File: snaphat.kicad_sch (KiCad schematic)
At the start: 94 parts, among them J1 Conn_01x08_S8B-PH-K-S(LF)(SN), J10 P70-6000045R, J11 P70-6000045R, J12 P70-6000045R, J2 Conn_02x20_2214SM-40G-75-PCR, J3 Conn_01x02_B2B-PH-K-S(LF)(SN), J4 USB_C_USB4930-00-A, J5 Conn_01x03_MC34747, J6 Conn_01x04_SFV4R-3STBE1HLF/C, J7 Conn_01x04_SFV4R-3STBE1HLF/C, J8 P70-6000045R, J9 P70-6000045R, Q1 Q_BC817-25, SW1 SW_B3FS-1050, SW2 SW_B3FS-1050, SW3 SW_B3FS-1050, SW4 SW_B3FS-1050, SW5 SW_B3FS-1050, SW6 SW_B3FS-1050, SW7 SW_B3FS-1050, SW8 SW_B3F-3150, U4 TPD2EUSB30DRTR, U6 LIS2DW12TR

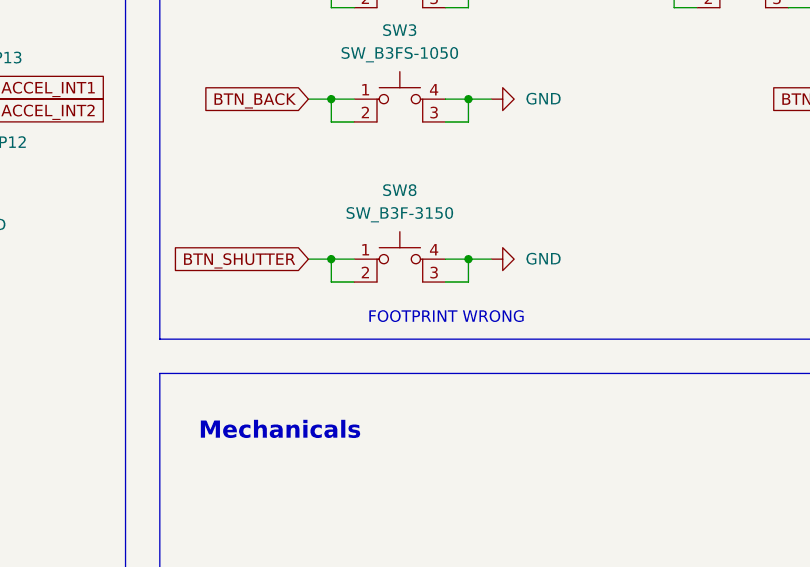
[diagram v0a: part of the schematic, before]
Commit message: Fix B3F-3150 symbol
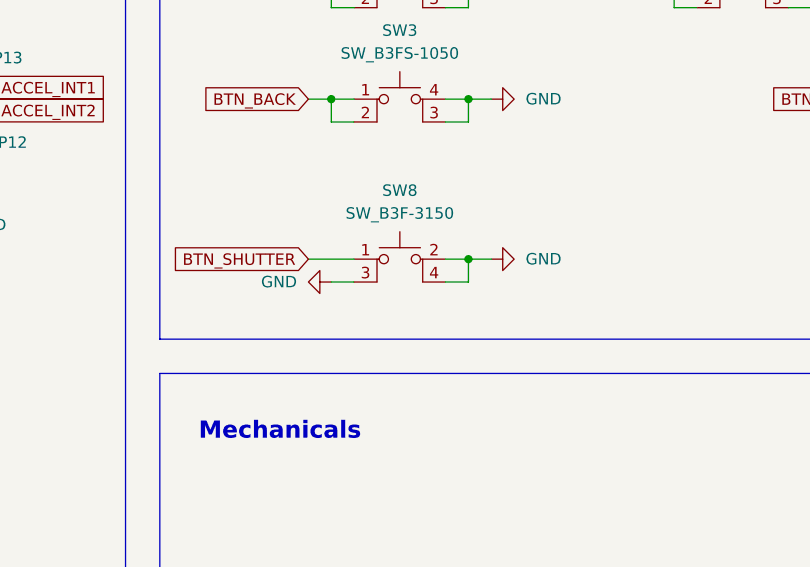
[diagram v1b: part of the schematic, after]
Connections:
- net BTN_SHUTTER: no longer SW8.2
- net GND: now also SW8.2
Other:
- note removed: "FOOTPRINT WRONG"
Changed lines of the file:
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@@
 		)
 	)
-	(text "FOOTPRINT WRONG"
-		(exclude_from_sim no)
-		(at 112.014 247.396 0)
-		(effects
-			(font
-				(face "Quicksand")
-				(size 1.27 1.27)
-				(thickness 0.1588)
-				(color 42 101 127 1)
-			)
-			(justify left bottom)
-		)
-	)
 	(text "GPIO9(MISO)\n"
 		(exclude_from_sim no)
@@
 	)
 	(junction
-		(at 107.95 240.03)
-		(diameter 0)
-		(color 38 87 104 1)
-	)
-	(junction
 		(at 69.85 213.36)
 		(diameter 0)
@@
 	(wire
 		(pts
-			(xy 105.41 240.03) (xy 107.95 240.03)
-		)
-		(stroke
-			(width 0)
-			(type solid)
-			(color 132 0 0 1)
-		)
-	)
-	(wire
-		(pts
 			(xy 284.48 67.31) (xy 287.02 67.31)
 		)
@@
 	(wire
 		(pts
-			(xy 107.95 240.03) (xy 110.49 240.03)
+			(xy 105.41 240.03) (xy 110.49 240.03)
 		)
 		(stroke
@@
 	(wire
 		(pts
-			(xy 107.95 242.57) (xy 107.95 240.03)
-		)
-		(stroke
-			(width 0)
-			(type solid)
-			(color 132 0 0 1)
-		)
-	)
-	(wire
-		(pts
 			(xy 93.98 86.36) (xy 111.76 86.36)
 		)
@@
 	)
 	(symbol
+		(lib_id "power:GND")
+		(at 107.95 242.57 270)
+		(unit 1)
+		(exclude_from_sim no)
+		(in_bom yes)
+		(on_board yes)
+		(dnp no)
+		(fields_autoplaced yes)
+		(property "Reference" "#PWR037"
+			(at 101.6 242.57 0)
+			(effects
+				(font
+					(face "Quicksand")
+					(size 1.27 1.27)
+					(color 42 101 127 1)
+				)
+				(hide yes)
+			)
+		)
+		(property "Value" "GND"
+			(at 104.14 242.5699 90)
+			(effects
+				(font
+					(face "Quicksand")
+					(size 1.27 1.27)
+					(color 42 101 127 1)
+				)
+				(justify right)
+			)
+		)
+		(property "Footprint" ""
+			(at 107.95 242.57 0)
+			(effects
+				(font
+					(face "Quicksand")
+					(size 1.27 1.27)
+					(color 42 101 127 1)
+				)
+				(hide yes)
+			)
+		)
+		(property "Datasheet" ""
+			(at 107.95 242.57 0)
+			(effects
+				(font
+					(face "Quicksand")
+					(size 1.27 1.27)
+					(color 42 101 127 1)
+				)
+				(hide yes)
+			)
+		)
+		(property "Description" "Power symbol creates a global label with name \"GND\" , ground"
+			(at 107.95 242.57 0)
+			(effects
+				(font
+					(face "Quicksand")
+					(size 1.27 1.27)
+					(color 42 101 127 1)
+				)
+				(hide yes)
+			)
+		)
+		(pin "1"
+		)
+		(instances
+			(project "snaphat"
+				(path "/1b9269fa-3ac8-429a-ab83-4cc9a4203d51"
+					(reference "#PWR037")
+					(unit 1)
+				)
+			)
+		)
+	)
+	(symbol
 		(lib_id "library:B32-2010")
 		(at 200.66 240.03 0)
@@
 	)
 	(symbol
+		(lib_id "library:SW_B3F-3150")
+		(at 115.57 240.03 0)
+		(unit 1)
+		(exclude_from_sim no)
+		(in_bom yes)
+		(on_board yes)
+		(dnp no)
+		(fields_autoplaced yes)
+		(property "Reference" "SW8"
+			(at 115.57 232.41 0)
+			(effects
+				(font
+					(size 1.27 1.27)
+				)
+			)
+		)
+		(property "Value" "SW_B3F-3150"
+			(at 115.57 234.95 0)
+			(effects
+				(font
+					(size 1.27 1.27)
+				)
+			)
+		)
+		(property "Footprint" "library:SW_B3F-3150"
+			(at 115.57 240.03 0)
+			(effects
+				(font
+					(size 1.27 1.27)
+				)
+				(hide yes)
+			)
+		)
+		(property "Datasheet" ""
+			(at 115.57 240.03 0)
+			(effects
+				(font
+					(size 1.27 1.27)
+				)
+				(hide yes)
+			)
+		)
+		(property "Description" "Tactile Switch, B3D Series, Side Actuated, Through Hole, Plunger for Cap, 100 gf, 50mA at 24VDC"
+			(at 115.57 240.03 0)
+			(effects
+				(font
+					(size 1.27 1.27)
+				)
+				(hide yes)
+			)
+		)
+		(property "Part number" "B3F-3150"
+			(at 115.57 240.03 0)
+			(effects
+				(font
+					(size 1.27 1.27)
+				)
+				(hide yes)
+			)
+		)
+		(property "Manufacturer" "OMRON"
+			(at 115.57 240.03 0)
+			(effects
+				(font
+					(size 1.27 1.27)
+				)
+				(hide yes)
+			)
+		)
+		(pin "3"
+		)
+		(pin "1"
+		)
+		(pin "2"
+		)
+		(pin "4"
+		)
+		(instances
+			(project ""
+				(path "/1b9269fa-3ac8-429a-ab83-4cc9a4203d51"
+					(reference "SW8")
+					(unit 1)
+				)
+			)
+		)
+	)
+	(symbol
 		(lib_id "library:1386735")
 		(at 186.69 267.97 0)
@@
 					(unit 1)
 				)
-			)
-		)
-	)
-	(symbol
-		(lib_id "library:SW_B3F-3150")
-		(at 115.57 242.57 0)
-		(unit 1)
-		(exclude_from_sim no)
-		(in_bom yes)
-		(on_board yes)
-		(dnp no)
-		(fields_autoplaced yes)
-		(property "Reference" "SW8"
-			(at 115.57 232.41 0)
-			(effects
-				(font
-					(face "Quicksand")
-					(size 1.27 1.27)
-					(color 42 101 127 1)
-				)
-			)
-		)
-		(property "Value" "SW_B3F-3150"
-			(at 115.57 234.95 0)
-			(effects
-				(font
-					(face "Quicksand")
-					(size 1.27 1.27)
-					(color 42 101 127 1)
-				)
-			)
-		)
-		(property "Footprint" "library:SW_B3F-3150"
-			(at 115.57 234.95 0)
-			(effects
-				(font
-					(face "Quicksand")
-					(size 1.27 1.27)
-					(color 42 101 127 1)
-				)
-				(hide yes)
-			)
-		)
-		(property "Datasheet" "http://www.apem.com/int/index.php?controller=attachment&id_attachment=1371"
-			(at 115.57 234.95 0)
-			(effects
-				(font
-					(face "Quicksand")
-					(size 1.27 1.27)
-					(color 42 101 127 1)
-				)
-				(hide yes)
-			)
-		)
-		(property "Description" "Tactile Switch, B3D Series, Side Actuated, Through Hole, Plunger for Cap, 100 gf, 50mA at 24VDC"
-			(at 115.57 242.57 0)
-			(effects
-				(font
-					(face "Quicksand")
-					(size 1.27 1.27)
-					(color 42 101 127 1)
-				)
-				(hide yes)
-			)
-		)
-		(property "Part number" "B3F-3150"
-			(at 115.57 242.57 0)
-			(effects
-				(font
-					(face "Quicksand")
-					(size 1.27 1.27)
-					(color 42 101 127 1)
-				)
-				(hide yes)
-			)
-		)
-		(property "Manufacturer" "OMRON"
-			(at 115.57 242.57 0)
-			(effects
-				(font
-					(face "Quicksand")
-					(size 1.27 1.27)
-					(color 42 101 127 1)
-				)
-				(hide yes)
-			)
-		)
-		(property "Part name" ""
-			(at 115.57 242.57 0)
-			(effects
-				(font
-					(size 1.27 1.27)
-				)
-			)
-		)
-		(pin "2"
-		)
-		(pin "3"
-		)
-		(pin "1"
-		)
-		(pin "4"
-		)
-		(instances
-			(project ""
-				(path "/1b9269fa-3ac8-429a-ab83-4cc9a4203d51"
-					(reference "SW8")
-					(unit 1)
-				)

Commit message: Fixes to power charger, cleanup schematic
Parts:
- added H15: 10304, library:Li-Pol_battery_8x30x40mm, symbol library:10304
- added H48, H49: SPH-002T-P0.5S, symbol library:SPH-002T-P0.5S
- added H50: PHR-2, symbol library:PHR-2
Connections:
- net BUZZER_SIGNAL is gone; now on net GND: J2.12 (Pin_12), R1.1
- net DISPLAY_BL is gone; now on net GND: J1.8 (Pin_8), J2.32 (Pin_32), R28.1
- net DISPLAY_DC is gone; now on net GND: J1.6 (Pin_6), J2.22 (Pin_22)
- net DISPLAY_RST is gone; now on net GND: J1.7 (Pin_7), J2.18 (Pin_18)
- net DISPLAY_SPI_CS is gone; now on net GND: J1.5 (Pin_5), J2.24 (Pin_24)
- net RPI_UART_RX is gone; now on net GND: J2.10 (Pin_10), J5.1 (Pin_1)
- net RPI_UART_TX is gone; now on net GND: J2.8 (Pin_8), J5.2 (Pin_2)
- net BTN_D: now also J2.27 (Pin_27); no longer J2.29 (Pin_29)
- net BTN_L: now also J2.29 (Pin_29); no longer J2.31 (Pin_31)
- net BTN_R: now also J2.31 (Pin_31); no longer J2.33 (Pin_33)
- net BTN_U: now also J2.33 (Pin_33); no longer J2.35 (Pin_35)
- net BTN_BACK renamed BTN_B
- net BTN_OK renamed BTN_A
- net DISPLAY_SPI_MOSI renamed DISPLAY_MOSI
- new net LOW_BATTERY: J2.35 (Pin_35)
- no-connect marks 10 -> 8
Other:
- note added: "Camera module:"
- note added: "Li-Po battery:"
- note added: "Raspberry Pi header"
- note added: "RaspberryPi spacers:"
- note added: "RaspberryPi:"
- note added: "USB-C and battery connector"
- note removed: "Raspberry Pi header and USB OTG"
- moved on the sheet: BZ1, C15, C19, C2, C20, C9, D1, D7, D8, H1, H10, H11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

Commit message: Start updating PCB, library fixes
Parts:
- removed H33: 9774100151R, library:Mounting_Wuerth_WA-SMSI-M2.5_H10mm_9774100151R, symbol library:9774100151R
- J4: footprint (none) -> library:USB_C_Receptacle_GCT_USB4105-xx-A_16P_TopMnt_Horizontal
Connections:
- net GND: now also J6.1 (Pin_1); no longer J6.4 (Pin_4)
- net GND_EXT: now also J7.1 (Pin_1); no longer J7.4 (Pin_4)
- net USBC_DATA_N: now also J6.3 (Pin_3); no longer J6.2 (Pin_2)
- net USBC_DATA_P: now also J6.2 (Pin_2); no longer J6.3 (Pin_3)
- net USBC_EXT_DATA_N: now also J7.3 (Pin_3); no longer J7.2 (Pin_2)
- net USBC_EXT_DATA_P: now also J7.2 (Pin_2); no longer J7.3 (Pin_3)
- net VBUS_EXT: now also J7.4 (Pin_4); no longer J7.1 (Pin_1)
- net BATTERY_N renamed Power supply/BATTERY_N
- net BATTERY_P renamed Power supply/BATTERY_P
- net PM_SCL renamed I2C_SCL
- net PM_SDA renamed I2C_SDA
- net VBUS renamed Power supply/VBUS
- net Power supply/VBUS: now also J6.4 (Pin_4); no longer J6.1 (Pin_1)
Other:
- sheet Power supply ports: added 3V3, 5V0, BATTERY_N, BATTERY_P, LOW_BATTERY, PM_SCL, PM_SDA, VBUS; removed none
- moved on the sheet: J7, SW1, SW2, SW3, SW4, SW5, SW6, SW7, SW8

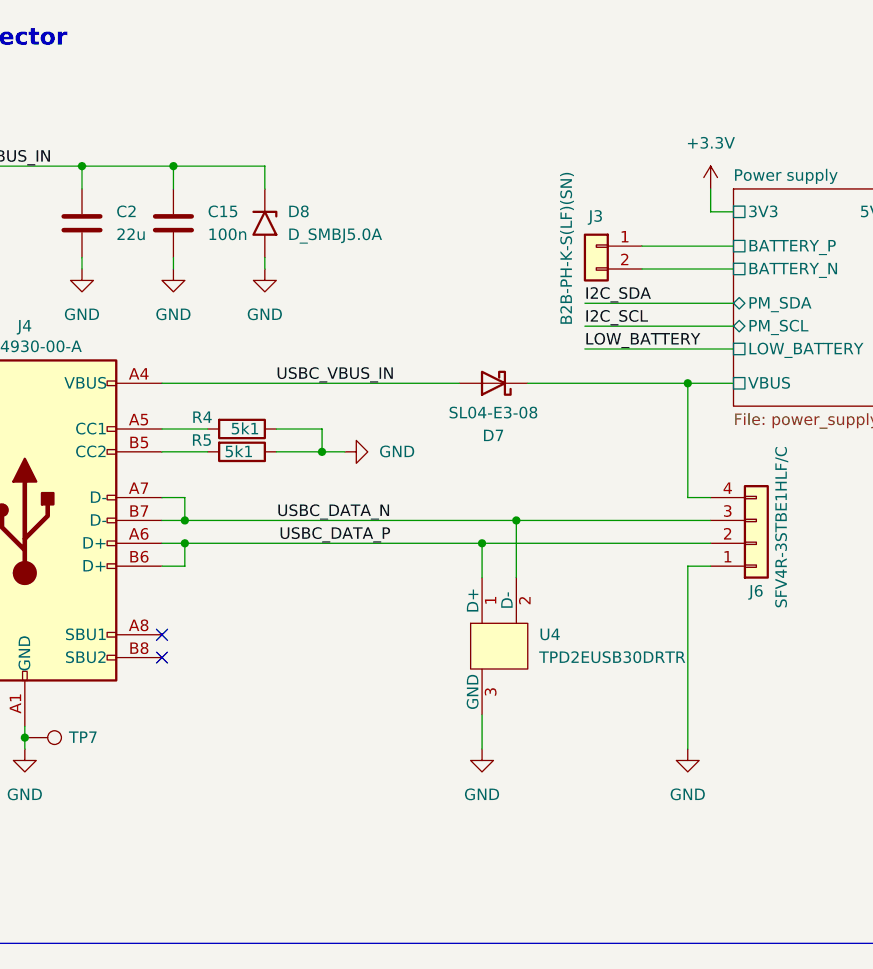
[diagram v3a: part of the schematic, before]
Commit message: Rerouted power and USB
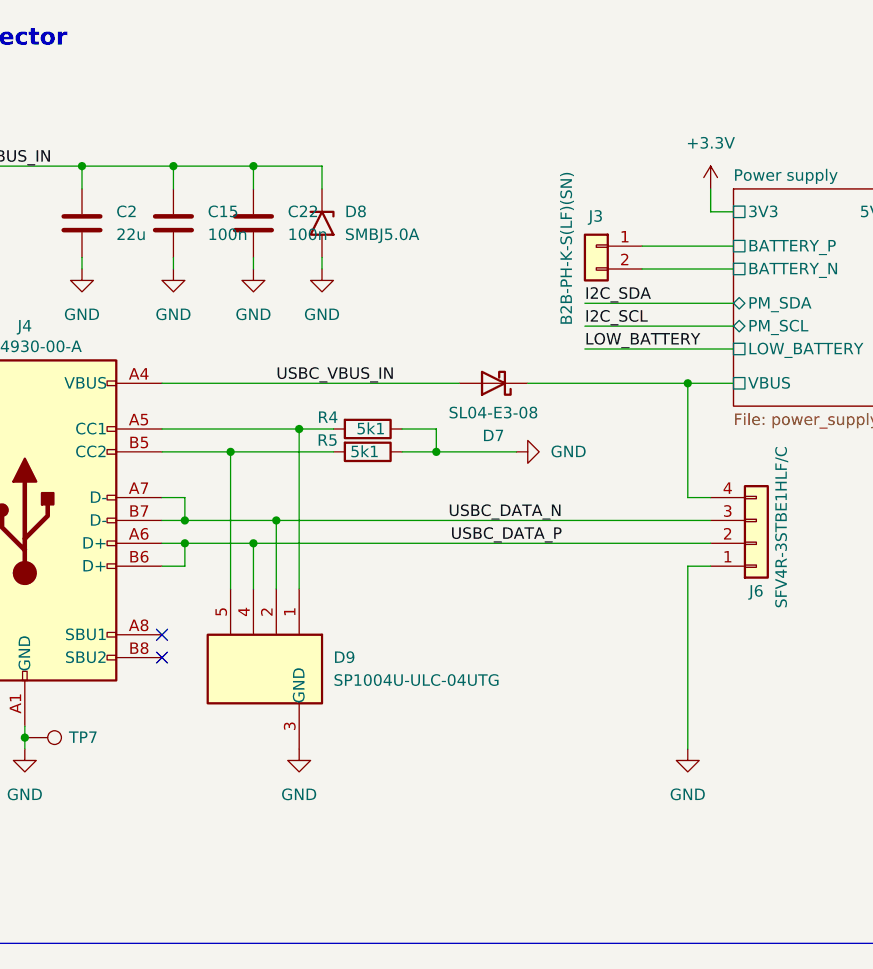
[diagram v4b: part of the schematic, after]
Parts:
- removed U4: TPD2EUSB30DRTR, library:Texas_DRT-3, symbol library:TPD2EUSB30DRTR
- added C22: 100n, library:C_0402_1005Metric, symbol library:C_100n_0402
- added D9: SP1004U-ULC-04UTG, library:SP1004UULC04UTG, symbol library:SP1004U-ULC-04UTG
- D8: footprint library:D_SMB -> library:SOD-123FL; symbol library:SMBJ5.0A -> library:D_SMF5.0A
- J1: footprint library:DW08R -> library:JST_S8B-PH-K-S_LF__SN_
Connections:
- net GND: now also C22.1, D9.3 (GND), D9.8 (GND_2)
- net USBC_DATA_N: now also D9.2, D9.9 (NC_3)
- net USBC_DATA_P: now also D9.4, D9.7 (NC_2)
- net USBC_VBUS_IN: now also C22.2
- net at J4.A5 (CC1), R4.2: now also D9.1, D9.10 (NC_4)
- net at J4.B5 (CC2), R5.2: now also D9.5, D9.6 (NC_1)
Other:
- moved on the sheet: D8, R4, R5

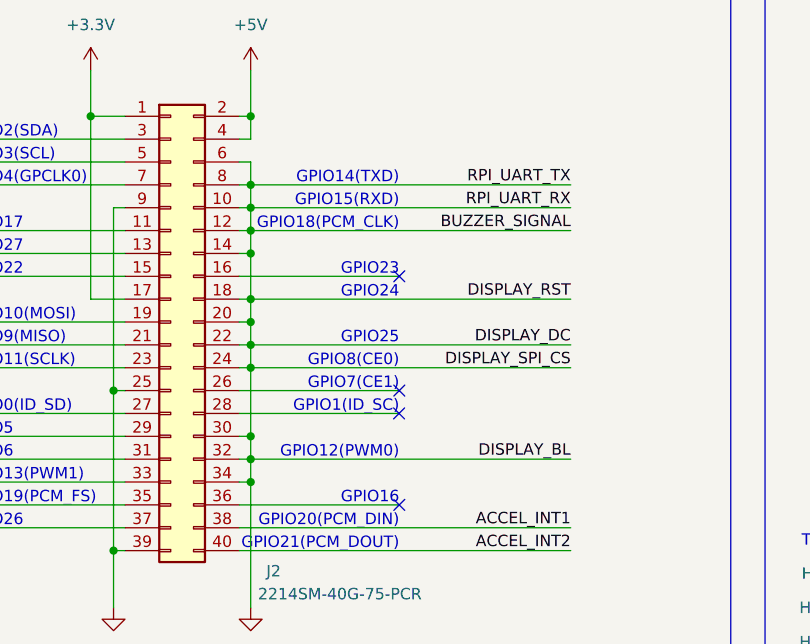
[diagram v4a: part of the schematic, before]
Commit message: Fix RPi connector on schematic, route rest of signals
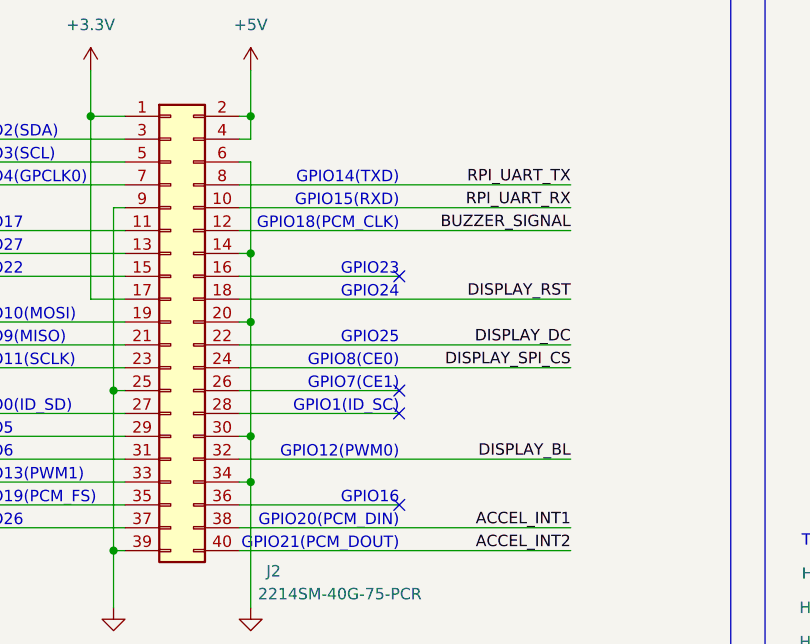
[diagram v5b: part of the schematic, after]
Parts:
- J1: footprint library:JST_S8B-PH-K-S_LF__SN_ -> library:DW08R
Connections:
- net GND: no longer J1.5 (Pin_5), J1.6 (Pin_6), J1.7 (Pin_7), J1.8 (Pin_8), J2.10 (Pin_10), J2.12 (Pin_12), J2.18 (Pin_18), J2.22 (Pin_22), J2.24 (Pin_24), J2.32 (Pin_32), J2.8 (Pin_8), J5.1 (Pin_1), J5.2 (Pin_2), R1.1, R28.1
- new net BUZZER_SIGNAL: J2.12 (Pin_12), R1.1
- new net DISPLAY_BL: J1.8 (Pin_8), J2.32 (Pin_32), R28.1
- new net DISPLAY_DC: J1.6 (Pin_6), J2.22 (Pin_22)
- new net DISPLAY_RST: J1.7 (Pin_7), J2.18 (Pin_18)
- new net DISPLAY_SPI_CS: J1.5 (Pin_5), J2.24 (Pin_24)
- new net RPI_UART_RX: J2.10 (Pin_10), J5.1 (Pin_1)
- new net RPI_UART_TX: J2.8 (Pin_8), J5.2 (Pin_2)
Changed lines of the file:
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@@
 	)
 	(junction
-		(at 161.29 173.99)
-		(diameter 0)
-		(color 0 0 0 0)
-	)
-	(junction
 		(at 143.51 166.37)
 		(diameter 0)
@@
 	)
 	(junction
-		(at 161.29 191.77)
-		(diameter 0)
-		(color 0 0 0 0)
-	)
-	(junction
 		(at 281.94 191.77)
 		(diameter 0)
@@
 	)
 	(junction
-		(at 161.29 179.07)
-		(diameter 0)
-		(color 0 0 0 0)
-	)
-	(junction
 		(at 378.46 199.39)
 		(diameter 0)
@@
 	)
 	(junction
-		(at 161.29 204.47)
-		(diameter 0)
-		(color 0 0 0 0)
-	)
-	(junction
 		(at 349.25 81.28)
 		(diameter 0)
@@
 	)
 	(junction
-		(at 161.29 194.31)
-		(diameter 0)
-		(color 0 0 0 0)
-	)
-	(junction
 		(at 68.58 175.26)
 		(diameter 0)
@@
 	)
 	(junction
-		(at 161.29 176.53)
-		(diameter 0)
-		(color 0 0 0 0)
-	)
-	(junction
 		(at 227.33 68.58)
 		(diameter 0)
@@
 	)
 	(junction
-		(at 161.29 186.69)
-		(diameter 0)
-		(color 0 0 0 0)
-	)
-	(junction
 		(at 68.58 172.72)
 		(diameter 0)
@@
 	(wire
 		(pts
-			(xy 161.29 191.77) (xy 160.02 191.77)
-		)
-		(stroke
-			(width 0)
-			(type solid)
-		)
-	)
-	(wire
-		(pts
-			(xy 161.29 179.07) (xy 161.29 181.61)
-		)
-		(stroke
-			(width 0)
-			(type solid)
-		)
-	)
-	(wire
-		(pts
 			(xy 378.46 196.85) (xy 378.46 199.39)
 		)
@@
 	(wire
 		(pts
-			(xy 161.29 173.99) (xy 160.02 173.99)
+			(xy 160.02 173.99) (xy 196.85 173.99)
 		)
 		(stroke
@@
 	(wire
 		(pts
-			(xy 161.29 181.61) (xy 161.29 186.69)
+			(xy 161.29 181.61) (xy 161.29 189.23)
 		)
 		(stroke
@@
 	(wire
 		(pts
-			(xy 161.29 176.53) (xy 160.02 176.53)
+			(xy 160.02 176.53) (xy 196.85 176.53)
 		)
 		(stroke
@@
 	(wire
 		(pts
-			(xy 161.29 189.23) (xy 161.29 191.77)
-		)
-		(stroke
-			(width 0)
-			(type solid)
-		)
-	)
-	(wire
-		(pts
 			(xy 35.56 180.34) (xy 33.02 180.34)
 		)
@@
 	(wire
 		(pts
-			(xy 161.29 194.31) (xy 160.02 194.31)
-		)
-		(stroke
-			(width 0)
-			(type solid)
-		)
-	)
-	(wire
-		(pts
 			(xy 284.48 213.36) (xy 284.48 210.82)
 		)
@@
 	(wire
 		(pts
-			(xy 161.29 173.99) (xy 196.85 173.99)
-		)
-		(stroke
-			(width 0)
-			(type solid)
-		)
-	)
-	(wire
-		(pts
 			(xy 214.63 36.83) (xy 214.63 39.37)
 		)
@@
 	(wire
 		(pts
-			(xy 161.29 176.53) (xy 161.29 179.07)
+			(xy 161.29 171.45) (xy 161.29 181.61)
 		)
 		(stroke
@@
 	(wire
 		(pts
-			(xy 161.29 186.69) (xy 160.02 186.69)
-		)
-		(stroke
-			(width 0)
-			(type solid)
-		)
-	)
-	(wire
-		(pts
 			(xy 255.27 144.78) (xy 269.24 144.78)
 		)
@@
 	(wire
 		(pts
-			(xy 161.29 173.99) (xy 161.29 176.53)
-		)
-		(stroke
-			(width 0)
-			(type solid)
-		)
-	)
-	(wire
-		(pts
 			(xy 269.24 147.32) (xy 266.7 147.32)
 		)
@@
 	(wire
 		(pts
-			(xy 161.29 186.69) (xy 196.85 186.69)
+			(xy 160.02 186.69) (xy 196.85 186.69)
 		)
 		(stroke
@@
 	(wire
 		(pts
-			(xy 161.29 204.47) (xy 160.02 204.47)
-		)
-		(stroke
-			(width 0)
-			(type solid)
-		)
-	)
-	(wire
-		(pts
 			(xy 281.94 39.37) (xy 281.94 41.91)
 		)
@@
 	(wire
 		(pts
-			(xy 161.29 194.31) (xy 196.85 194.31)
+			(xy 160.02 194.31) (xy 196.85 194.31)
 		)
 		(stroke
@@
 	(wire
 		(pts
-			(xy 161.29 179.07) (xy 196.85 179.07)
-		)
-		(stroke
-			(width 0)
-			(type solid)
-		)
-	)
-	(wire
-		(pts
 			(xy 107.95 184.15) (xy 147.32 184.15)
 		)
@@
 	(wire
 		(pts
-			(xy 161.29 176.53) (xy 196.85 176.53)
-		)
-		(stroke
-			(width 0)
-			(type solid)
-		)
-	)
-	(wire
-		(pts
 			(xy 88.9 62.23) (xy 114.3 62.23)
 		)
@@
 	(wire
 		(pts
-			(xy 161.29 171.45) (xy 161.29 173.99)
-		)
-		(stroke
-			(width 0)
-			(type solid)
-		)
-	)
-	(wire
-		(pts
 			(xy 199.39 73.66) (xy 199.39 76.2)
 		)
@@
 	(wire
 		(pts
-			(xy 161.29 201.93) (xy 161.29 204.47)
+			(xy 161.29 201.93) (xy 161.29 207.01)
 		)
 		(stroke
@@
 	(wire
 		(pts
-			(xy 161.29 191.77) (xy 161.29 194.31)
-		)
-		(stroke
-			(width 0)
-			(type solid)
-		)
-	)
-	(wire
-		(pts
-			(xy 161.29 191.77) (xy 196.85 191.77)
+			(xy 160.02 191.77) (xy 196.85 191.77)
 		)
 		(stroke
@@
 	(wire
 		(pts
-			(xy 161.29 204.47) (xy 161.29 207.01)
-		)
-		(stroke
-			(width 0)
-			(type solid)
-		)
-	)
-	(wire
-		(pts
 			(xy 161.29 161.29) (xy 161.29 166.37)
 		)
@@
 	(wire
 		(pts
-			(xy 161.29 186.69) (xy 161.29 189.23)
-		)
-		(stroke
-			(width 0)
-			(type solid)
-		)
-	)
-	(wire
-		(pts
 			(xy 196.85 78.74) (xy 199.39 78.74)
 		)
@@
 	(wire
 		(pts
-			(xy 161.29 204.47) (xy 196.85 204.47)
+			(xy 160.02 204.47) (xy 196.85 204.47)
 		)
 		(stroke
@@
 	(wire
 		(pts
-			(xy 161.29 179.07) (xy 160.02 179.07)
+			(xy 160.02 179.07) (xy 196.85 179.07)
 		)
 		(stroke
@@
 	(wire
 		(pts
-			(xy 161.29 194.31) (xy 161.29 201.93)
+			(xy 161.29 189.23) (xy 161.29 201.93)
 		)
 		(stroke
@@
 			)
 		)
-		(property "Footprint" "library:JST_S8B-PH-K-S_LF__SN_"
+		(property "Footprint" "library:DW08R"
 			(at 83.82 54.61 0)
 			(effects
